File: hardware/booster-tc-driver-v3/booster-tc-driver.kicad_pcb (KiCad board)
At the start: 4 copper layers, 53.3 x 72 mm, 126 parts, among them IC1 CAT4109V-GT2, IC2 LDL1117S50R, IC4 UCC27524AQDRQ1, IC5 UCC27524AQDRQ1, J1 62201021121, J10 22-23-2021, J2 EHT-105-01-S-D, J3 22-23-2021, J4 3-647166-2, J5 3-647166-2, J6 3-647166-2, J7 3-647166-2, J8 3-647166-2, J9 22-23-2021, Q1 T2N7002AK, Q2 BUK9M5R2-30EX, SW1 SW_SPDT, U1 IF-D95T << must be T, U10 SQJ500AEP-T1_GE3, U11 SQJ500AEP-T1_GE3, U12 SQJ500AEP-T1_GE3, U13 SQJ500AEP-T1_GE3, U2 IF-E96E, U3 IF-D95T << must be T, U4 CSTNE8M00G550000R0, U5 STM32G474CBTx, U6 MCP9700Ax-ETT, U7 AP1501A-12K5G-13, U8 LT1963AxST-3.3

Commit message: v3
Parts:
- removed D16: 1N5819HW-7-F, digikey-footprints:SOD-123
- removed J8: 3-647166-2, Library:36471662
- added C13: .1uf, Capacitor_SMD:C_0603_1608Metric_Pad1.08x0.95mm_HandSolder, B.Cu at (44.5, 63.8)
- added J11: 3-647166-5, Library:36471665, F.Cu at (59.5, 65.2)
- moved J4 148.1 mm to (24.0, 58.0), turned to 180 degrees
- moved J1 146.4 mm to (33.3, 49.4)
- moved U5 135.7 mm to (36.0, 58.2)
- moved C6 119.0 mm to (28.0, 73.0), turned to -90 degrees
- moved C2 116.8 mm to (29.2, 55.8), turned to 90 degrees
- moved C5 115.4 mm to (31.2, 68.2), turned to -90 degrees
- moved C7 114.4 mm to (31.2, 64.8), turned to 90 degrees
- moved C8 112.6 mm to (32.8, 55.8), turned to 90 degrees
- moved C9 112.4 mm to (33.0, 64.8), turned to 90 degrees
- moved C10 110.6 mm to (34.8, 64.8), turned to 90 degrees
- moved C26 110.5 mm to (31.0, 53.2)
- moved R5 109.7 mm to (26.0, 73.0), turned to 90 degrees
- moved C16 106.6 mm to (37.5, 71.6)
- moved C14 106.4 mm to (37.5, 68.0), turned to 0 degrees
- moved C17 105.7 mm to (37.5, 69.8), turned to 0 degrees
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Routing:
- net GND: track 93.3 -> 160.5 mm, vias 78 -> 97
- net +24V: track 49.7 -> 106.7 mm, vias 9 -> 8
- net THERM1: track 0.00 -> 52.3 mm, vias 0 -> 3
- net VAC_IN: track 0.00 -> 51.0 mm, vias 0 -> 1
- net SCR: track 0.00 -> 48.3 mm, vias 0 -> 2
- net VDD: track 13.6 -> 59.9 mm, vias 3 -> 9
- net THERM2: track 0.00 -> 45.4 mm, vias 0 -> 3
- net PFC: track 0.00 -> 44.0 mm
- net LED_I_IN: track 0.00 -> 39.9 mm, vias 0 -> 1
- net LED_TMP: track 0.00 -> 38.0 mm, vias 0 -> 1
- net LED_VBUS: track 0.00 -> 36.0 mm, vias 0 -> 1
- net THERM_BOARD: track 2.27 -> 35.1 mm, vias 0 -> 1
- net I_L_IN: track 0.00 -> 32.7 mm, vias 0 -> 1
- net USART_RX: track 8.75 -> 38.3 mm, vias 0 -> 1
- net MODE_IN: track 0.00 -> 24.9 mm, vias 0 -> 1
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
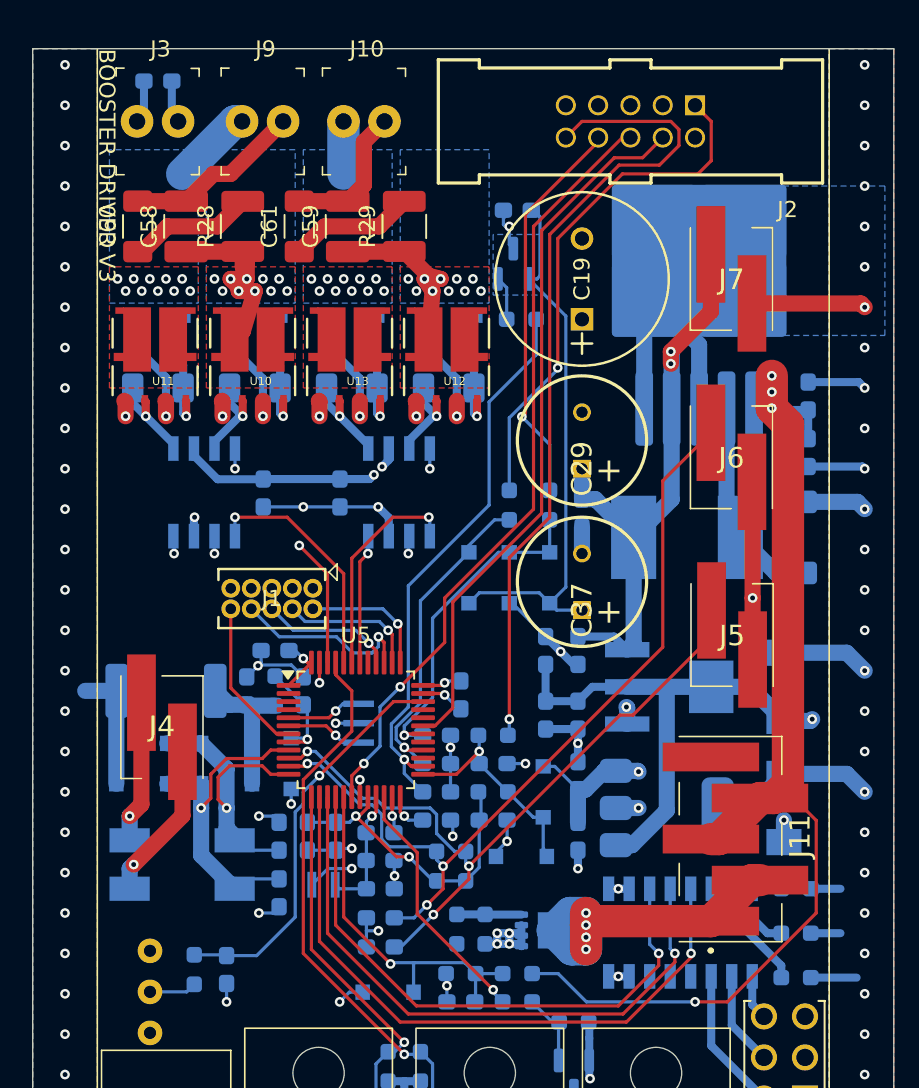
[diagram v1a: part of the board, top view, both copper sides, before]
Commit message: v3 front silkscreen
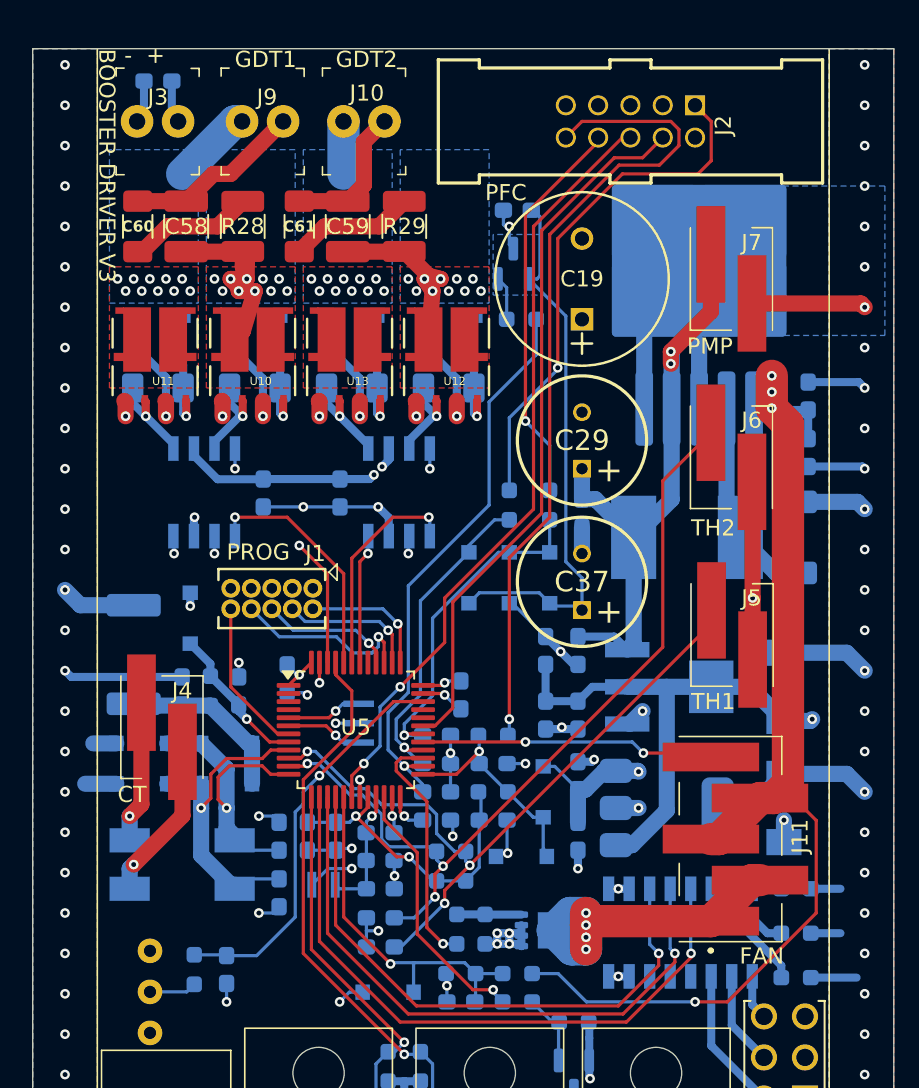
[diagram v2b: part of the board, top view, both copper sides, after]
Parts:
- moved D6 11.0 mm to (25.8, 51.2), turned to -90 degrees
- moved C2 4.00 mm to (25.2, 55.8)
- moved C8 4.00 mm to (28.8, 55.8)
- moved R7 4.00 mm to (27.0, 55.8)
- moved R6 3.01 mm to (22.2, 53.5), turned to 90 degrees
- moved C26 1.90 mm to (31.8, 55.0), turned to -90 degrees
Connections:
- U5 pad 27: unconnected-(U5-PB13-Pad27) -> FAN_EN
- U5 pad 29: unconnected-(U5-PB15-Pad29) -> FAN_PWM
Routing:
- net FAN_PWM: track 0.00 -> 18.2 mm, vias 0 -> 2
- net FAN_EN: track 0.00 -> 15.1 mm, vias 0 -> 1
- net GND: track 160.5 -> 165.0 mm, vias 97 -> 99
- net I_PRI: track 7.00 -> 9.30 mm
- net Net-(C2-Pad1): track 9.10 -> 10.8 mm
- net USART_TX: track 15.7 -> 16.4 mm
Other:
- board text added: "- +"
- board text added: "CT"
- board text added: "FAN"
- board text added: "GDT1"
- board text added: "GDT2"
- board text added: "PFC"
- board text added: "PMP"
- board text added: "PROG"
- board text added: "TH1"
- board text added: "TH2"

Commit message: pfc v3
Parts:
- added R23: 1k, Resistor_SMD:R_0603_1608Metric_Pad0.98x0.95mm_HandSolder, B.Cu at (44.2, 56.0)
- added R30: 100R, Resistor_SMD:R_0603_1608Metric_Pad0.98x0.95mm_HandSolder, B.Cu at (39.0, 53.5)
- moved D15 1.75 mm to (36.5, 73.5)
- moved C53 0.14 mm to (35.0, 43.6)
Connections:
- J2 pad 04: PFC -> Net-(J2-Pad04)
- J2 pad 06: SCR -> Net-(J2-Pad06)
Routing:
- net PFC: track 44.0 -> 4.50 mm, vias 0 -> 1
- net Net-(J2-Pad04): track 0.00 -> 39.2 mm, vias 0 -> 1
- net SCR: track 48.3 -> 9.26 mm, vias 2 -> 1
- net Net-(J2-Pad06): track 0.00 -> 38.0 mm, vias 0 -> 1
- net GND: track 165.0 -> 159.5 mm
- net +5V: track 156.0 -> 161.4 mm
- net 24V_SENSE: track 22.4 -> 21.4 mm
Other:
- board text added: "D13"
- board text added: "D14"

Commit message: pfc v3 finalized
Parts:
- removed C13: .1uf, Capacitor_SMD:C_0603_1608Metric_Pad1.08x0.95mm_HandSolder
- removed D10, D7: 1N5819HW-7-F, digikey-footprints:SOD-123
- removed R10: 1k, Resistor_SMD:R_0603_1608Metric_Pad0.98x0.95mm_HandSolder
- J2: value EHT-105-01-S-D -> 61201021621; footprint Library:SAMTEC_EHT-105-01-S-D -> Connector_IDC:IDC-Header_2x05_P2.54mm_Vertical
- moved R1 17.6 mm to (45.0, 61.8)
- moved D1 15.1 mm to (47.2, 63.2), turned to -90 degrees
- moved D8 13.5 mm to (42.0, 49.8)
- moved R9 10.3 mm to (44.0, 48.2), turned to 90 degrees
- moved C11 9.02 mm to (45.8, 50.8), turned to -90 degrees
- moved C12 8.51 mm to (44.0, 51.8), turned to -90 degrees
- moved C3 6.40 mm to (45.0, 65.2), turned to -90 degrees
- moved J2 5.56 mm to (58.5, 19.7), turned to -90 degrees
- moved R23 4.14 mm to (40.5, 54.2)
- moved R11 3.82 mm to (45.8, 47.3)
- moved C19 1.25 mm to (50.0, 34.0)
- moved J7 1.25 mm to (59.2, 31.5)
- moved J5 1.23 mm to (59.3, 53.5)
- moved J6 1.23 mm to (59.2, 42.5)
- moved J11 1.11 mm to (59.5, 66.4)
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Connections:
- R23 pad 1: Net-(J2-Pad04) -> Net-(J2-Pin_4)
- R30 pad 1: Net-(J2-Pad06) -> Net-(J2-Pin_6)
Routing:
- net Net-(J2-Pad04): track 39.2 -> 0.00 mm, vias 1 -> 0
- net Net-(J2-Pad06): track 38.0 -> 0.00 mm, vias 1 -> 0
- net Net-(J2-Pin_4): track 0.00 -> 37.8 mm, vias 0 -> 1
- net Net-(J2-Pin_6): track 0.00 -> 36.3 mm, vias 0 -> 1
- net VAC_IN: track 51.0 -> 26.9 mm
- net I_L_IN: track 32.7 -> 44.6 mm
- net I_L: track 20.5 -> 12.0 mm, vias 1 -> 2
- net VDD: track 59.5 -> 53.2 mm, vias 9 -> 11
- net VREF: track 19.2 -> 13.2 mm
- net +5V: track 161.4 -> 158.1 mm
- net VAC_SENSE: track 13.5 -> 16.6 mm
- net VBUS_SENSE: track 21.3 -> 18.4 mm, vias 1 -> 2
- net VBUS_IN: track 24.3 -> 26.5 mm
- net LED_VBUS: track 36.0 -> 34.4 mm
- net LED_TMP: track 38.0 -> 36.7 mm
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
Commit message: idk
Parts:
- moved C11 5.22 mm to (45.0, 56.0)
- moved R11 5.22 mm to (45.0, 52.5)
- moved D8 3.08 mm to (38.9, 49.8), turned to 0 degrees
- moved R23 3.00 mm to (40.5, 57.2)
- moved C12 1.68 mm to (42.5, 52.5)
- moved R9 1.68 mm to (42.5, 49.0)
- moved D9 0.53 mm to (47.5, 49.0)
- turned D13 to -90 degrees
- turned D14 to -90 degrees
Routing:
- net VBUS_IN: track 26.5 -> 32.3 mm
- net VBUS_SENSE: track 18.4 -> 13.9 mm
- net VDD: track 53.2 -> 57.3 mm, vias 11 -> 10
- net Net-(J2-Pin_4): track 37.8 -> 40.8 mm
- net VAC_IN: track 26.9 -> 28.3 mm
- net PFC: track 3.98 -> 2.94 mm
- net GND: track 160.4 -> 161.3 mm
- net VAC_SENSE: track 16.6 -> 16.0 mm
- net +12V: vias 4 -> 3
